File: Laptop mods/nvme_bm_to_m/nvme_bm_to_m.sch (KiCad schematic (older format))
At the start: 9 parts, among them J1 USB, U1 NGFF_M, U2 NGFF_B

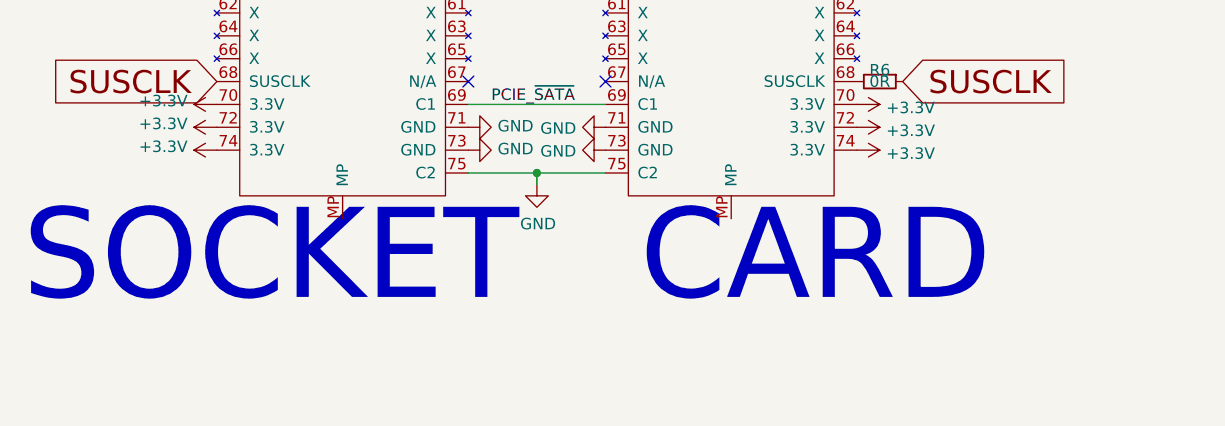
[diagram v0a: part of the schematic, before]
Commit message: Adding GND to the NVMe BM to M card shield
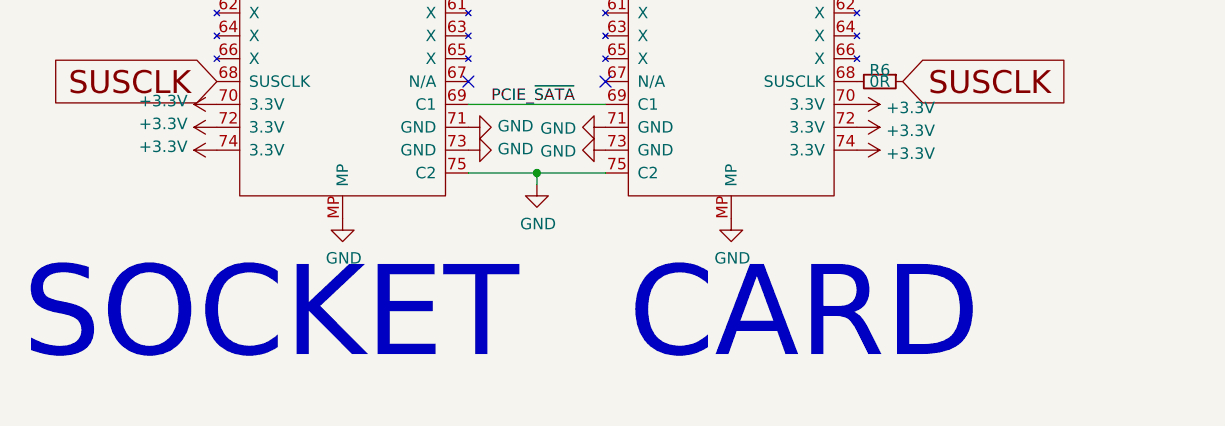
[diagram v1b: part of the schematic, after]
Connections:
- net GND: now also U1.MP, U2.MP
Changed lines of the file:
@@
 	0    -1   -1   0
 $EndComp
-Text Notes 3650 5950 0    394  ~ 0
+Text Notes 3600 6200 0    394  ~ 0
 CARD
-Text Notes 950  5950 0    394  ~ 0
+Text Notes 950  6200 0    394  ~ 0
 SOCKET
 Text GLabel 1800 3450 0    50   Input ~ 0
@@
 Text GLabel 5800 2200 0    50   Input ~ 0
 D+
+$Comp
+L power:GND #PWR?
+U 1 1 6172BF5C
+P 2350 5550
+F 0 "#PWR?" H 2350 5300 50  0001 C CNN
+F 1 "GND" H 2355 5377 50  0000 C CNN
+F 2 "" H 2350 5550 50  0001 C CNN
+F 3 "" H 2350 5550 50  0001 C CNN
+	1    2350 5550
+	1    0    0    -1
+$EndComp
+$Comp
+L power:GND #PWR?
+U 1 1 6172C327
+P 4050 5550
+F 0 "#PWR?" H 4050 5300 50  0001 C CNN
+F 1 "GND" H 4055 5377 50  0000 C CNN
+F 2 "" H 4050 5550 50  0001 C CNN
+F 3 "" H 4050 5550 50  0001 C CNN
+	1    4050 5550
+	1    0    0    -1
+$EndComp
 $EndSCHEMATC

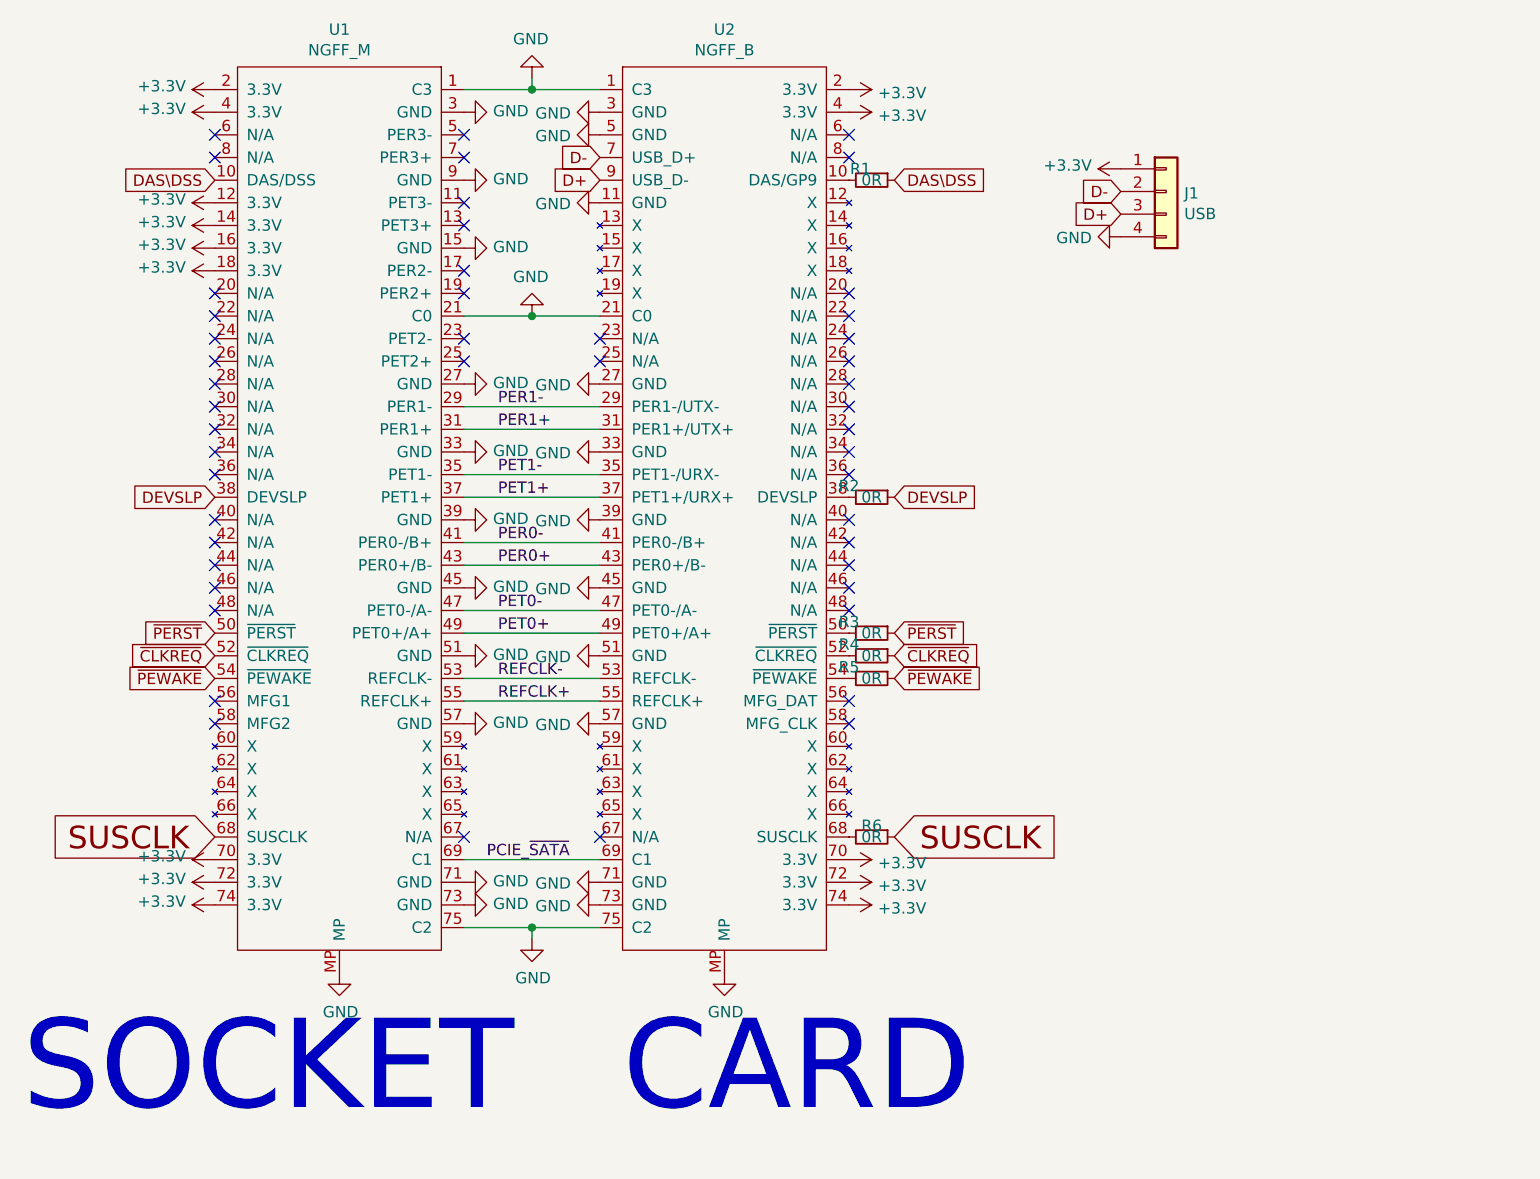
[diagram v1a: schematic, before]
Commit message: Rerouted diffpairs to NVMe BM to M adapter, made the adapter longer, added holes so that part of the adapter can be snipped off for length decrease
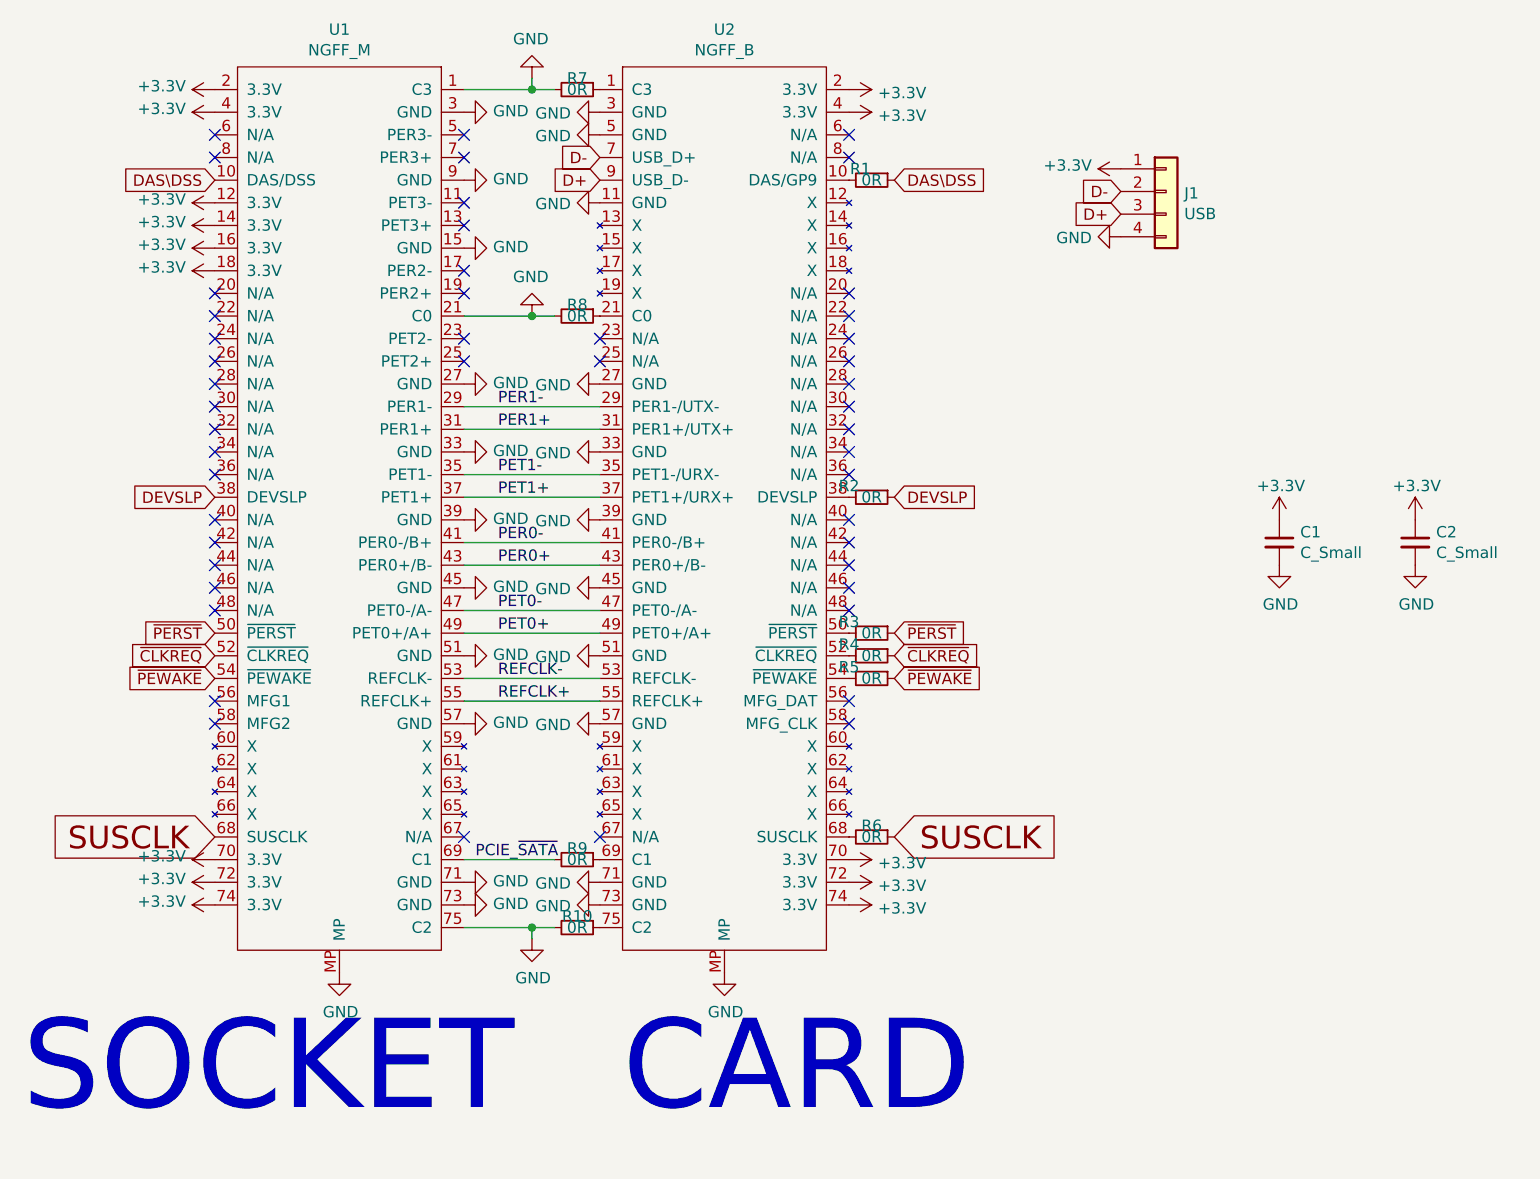
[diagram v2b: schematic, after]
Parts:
- added C1, C2: C_Small, Capacitor_SMD:C_1206_3216Metric_Pad1.33x1.80mm_HandSolder, symbol Device:C_Small
- added R10, R7, R8, R9: 0R, Resistor_SMD:R_0402_1005Metric, symbol Device:R_Small
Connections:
- net +3V3: now also C1.1, C2.1
- net GND: now also C1.2, C2.2, R10.2, R7.2, R8.2; no longer U2.1 (C3), U2.21 (C0), U2.75 (C2)
- net PCIE_~SATA: now also R9.2; no longer U2.69 (C1)
- new net: R7.1, U2.1 (C3)
- new net: R8.1, U2.21 (C0)
- new net: R9.1, U2.69 (C1)
- new net: R10.1, U2.75 (C2)
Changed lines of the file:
@@
 	0    -1   -1   0
 $EndComp
-Wire Wire Line
-	3500 5050 2900 5050
 $Comp
 L power:GND #PWR0114
@@
 $EndComp
 Wire Wire Line
-	2900 2650 3200 2650
-Wire Wire Line
-	3200 2650 3500 2650
+	3200 2650 3300 2650
 Connection ~ 3200 2650
-Wire Wire Line
-	2900 1650 3200 1650
 Wire Wire Line
 	3200 1650 3200 1600
 Connection ~ 3200 1650
 Wire Wire Line
-	3200 1650 3500 1650
+	3200 1650 3300 1650
 $Comp
 L power:GND #PWR0123
@@
 Text GLabel 4800 4950 2    100  Input ~ 0
 SUSCLK
-Text Label 3000 5050 0    50   ~ 0
-PCIE_~SATA
 Text Label 3050 4350 0    50   ~ 0
 REFCLK+
@@
 PER1-
 Wire Wire Line
-	3500 5350 3200 5350
-Wire Wire Line
 	3200 5400 3200 5350
 Connection ~ 3200 5350
-Wire Wire Line
-	3200 5350 2900 5350
 $Comp
 L Device:R_Small R1
@@
 D+
 $Comp
-L power:GND #PWR?
+L power:GND #PWR0142
 U 1 1 6172BF5C
 P 2350 5550
-F 0 "#PWR?" H 2350 5300 50  0001 C CNN
+F 0 "#PWR0142" H 2350 5300 50  0001 C CNN
 F 1 "GND" H 2355 5377 50  0000 C CNN
 F 2 "" H 2350 5550 50  0001 C CNN
@@
 $EndComp
 $Comp
-L power:GND #PWR?
+L power:GND #PWR0143
 U 1 1 6172C327
 P 4050 5550
-F 0 "#PWR?" H 4050 5300 50  0001 C CNN
+F 0 "#PWR0143" H 4050 5300 50  0001 C CNN
 F 1 "GND" H 4055 5377 50  0000 C CNN
 F 2 "" H 4050 5550 50  0001 C CNN
@@
 	1    0    0    -1
 $EndComp
+Wire Wire Line
+	2900 1650 3200 1650
+Wire Wire Line
+	2900 2650 3200 2650
+Text Label 2950 5050 0    50   ~ 0
+PCIE_~SATA
+Wire Wire Line
+	3200 5350 2900 5350
+$Comp
+L Device:R_Small R9
+U 1 1 617EE876
+P 3400 5050
+F 0 "R9" V 3350 5050 50  0000 C CNN
+F 1 "0R" V 3400 5050 50  0000 C CNN
+F 2 "Resistor_SMD:R_0402_1005Metric" H 3400 5050 50  0001 C CNN
+F 3 "~" H 3400 5050 50  0001 C CNN
+	1    3400 5050
+	0    1    1    0
+$EndComp
+Wire Wire Line
+	3300 5050 2900 5050
+$Comp
+L Device:R_Small R8
+U 1 1 617F13B9
+P 3400 2650
+F 0 "R8" V 3350 2650 50  0000 C CNN
+F 1 "0R" V 3400 2650 50  0000 C CNN
+F 2 "Resistor_SMD:R_0402_1005Metric" H 3400 2650 50  0001 C CNN
+F 3 "~" H 3400 2650 50  0001 C CNN
+	1    3400 2650
+	0    1    1    0
+$EndComp
+$Comp
+L Device:R_Small R7
+U 1 1 617F3029
+P 3400 1650
+F 0 "R7" V 3350 1650 50  0000 C CNN
+F 1 "0R" V 3400 1650 50  0000 C CNN
+F 2 "Resistor_SMD:R_0402_1005Metric" H 3400 1650 50  0001 C CNN
+F 3 "~" H 3400 1650 50  0001 C CNN
+	1    3400 1650
+	0    1    1    0
+$EndComp
+$Comp
+L Device:R_Small R10
+U 1 1 617F3CD3
+P 3400 5350
+F 0 "R10" V 3350 5350 50  0000 C CNN
+F 1 "0R" V 3400 5350 50  0000 C CNN
+F 2 "Resistor_SMD:R_0402_1005Metric" H 3400 5350 50  0001 C CNN
+F 3 "~" H 3400 5350 50  0001 C CNN
+	1    3400 5350
+	0    1    1    0
+$EndComp
+Wire Wire Line
+	3300 5350 3200 5350
+$Comp
+L Device:C_Small C1
+U 1 1 617FE3CB
+P 6500 3650
+F 0 "C1" H 6592 3696 50  0000 L CNN
+F 1 "C_Small" H 6592 3605 50  0000 L CNN
+F 2 "Capacitor_SMD:C_1206_3216Metric_Pad1.33x1.80mm_HandSolder" H 6500 3650 50  0001 C CNN
+F 3 "~" H 6500 3650 50  0001 C CNN
+	1    6500 3650
+	1    0    0    -1
+$EndComp
+$Comp
+L Device:C_Small C2
+U 1 1 617FEC6E
+P 7100 3650
+F 0 "C2" H 7192 3696 50  0000 L CNN
+F 1 "C_Small" H 7192 3605 50  0000 L CNN
+F 2 "Capacitor_SMD:C_1206_3216Metric_Pad1.33x1.80mm_HandSolder" H 7100 3650 50  0001 C CNN
+F 3 "~" H 7100 3650 50  0001 C CNN
+	1    7100 3650
+	1    0    0    -1
+$EndComp
+$Comp
+L power:GND #PWR0144
+U 1 1 61801303
+P 6500 3750
+F 0 "#PWR0144" H 6500 3500 50  0001 C CNN
+F 1 "GND" H 6505 3577 50  0000 C CNN
+F 2 "" H 6500 3750 50  0001 C CNN
+F 3 "" H 6500 3750 50  0001 C CNN
+	1    6500 3750
+	1    0    0    -1
+$EndComp
+$Comp
+L power:GND #PWR0145
+U 1 1 61802B53
+P 7100 3750
+F 0 "#PWR0145" H 7100 3500 50  0001 C CNN
+F 1 "GND" H 7105 3577 50  0000 C CNN
+F 2 "" H 7100 3750 50  0001 C CNN
+F 3 "" H 7100 3750 50  0001 C CNN
+	1    7100 3750
+	1    0    0    -1
+$EndComp
+$Comp
+L power:+3.3V #PWR0146
+U 1 1 61805095
+P 6500 3550
+F 0 "#PWR0146" H 6500 3400 50  0001 C CNN
+F 1 "+3.3V" H 6400 3700 50  0000 L CNN
+F 2 "" H 6500 3550 50  0001 C CNN
+F 3 "" H 6500 3550 50  0001 C CNN
+	1    6500 3550
+	1    0    0    -1
+$EndComp
+$Comp
+L power:+3.3V #PWR0147
+U 1 1 61806484
+P 7100 3550
+F 0 "#PWR0147" H 7100 3400 50  0001 C CNN
+F 1 "+3.3V" H 7000 3700 50  0000 L CNN
+F 2 "" H 7100 3550 50  0001 C CNN
+F 3 "" H 7100 3550 50  0001 C CNN
+	1    7100 3550
+	1    0    0    -1
+$EndComp
